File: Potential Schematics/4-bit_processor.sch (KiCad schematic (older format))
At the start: 0 parts

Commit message: Made Full ALU
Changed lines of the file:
@@
 $Descr A4 11693 8268
 encoding utf-8
-Sheet 1 6
+Sheet 1 22
 Title "4-bit_processor"
 Date "2018-09-11"
@@
 $EndDescr
 $Sheet
-S 1900 1250 750  1000
-U 5B990C59
-F0 "Full_ALU" 60
-F1 "Full_ALU.sch" 60
+S 1100 1200 3300 2300
+U 5B9D167A
+F0 "CPU" 60
+F1 "CPU.sch" 60
 $EndSheet
 $EndSCHEMATC

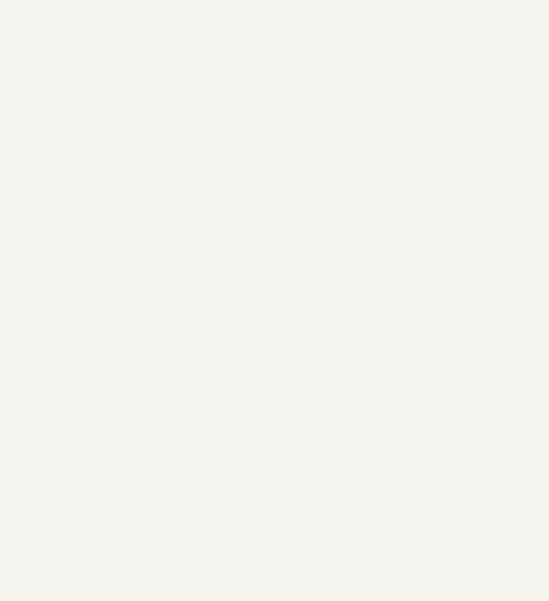
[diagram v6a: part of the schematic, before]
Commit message: Updated overview of Schematic
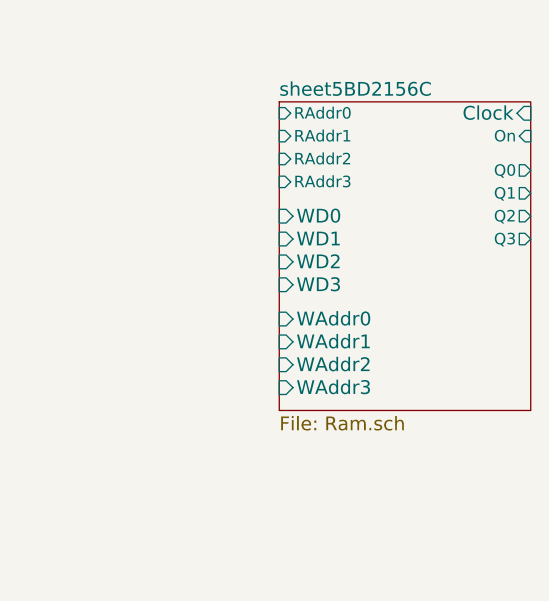
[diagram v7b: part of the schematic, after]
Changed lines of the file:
@@
 $Descr A4 11693 8268
 encoding utf-8
-Sheet 1 467
+Sheet 1 902
 Title "4-bit_processor"
 Date "2018-09-14"
@@
 F1 "CPU.sch" 60
 $EndSheet
+$Sheet
+S 6400 1450 1100 1350
+U 5BD21588
+F0 "sheet5BD2156C" 60
+F1 "Ram.sch" 60
+F2 "Clock" I R 7500 1500 60
+F3 "WD0" I L 6400 1950 60
+F4 "WD1" I L 6400 2050 60
+F5 "WD2" I L 6400 2150 60
+F6 "WD3" I L 6400 2250 60
+F7 "WAddr0" I L 6400 2400 60
+F8 "WAddr1" I L 6400 2500 60
+F9 "WAddr2" I L 6400 2600 60
+F10 "WAddr3" I L 6400 2700 60
+F11 "RAddr0" I L 6400 1500 50
+F12 "RAddr1" I L 6400 1600 50
+F13 "RAddr2" I L 6400 1700 50
+F14 "RAddr3" I L 6400 1800 50
+F15 "Q0" O R 7500 1750 50
+F16 "Q1" O R 7500 1850 50
+F17 "Q2" O R 7500 1950 50
+F18 "Q3" O R 7500 2050 50
+F19 "On" I R 7500 1600 50
+$EndSheet
 $EndSCHEMATC

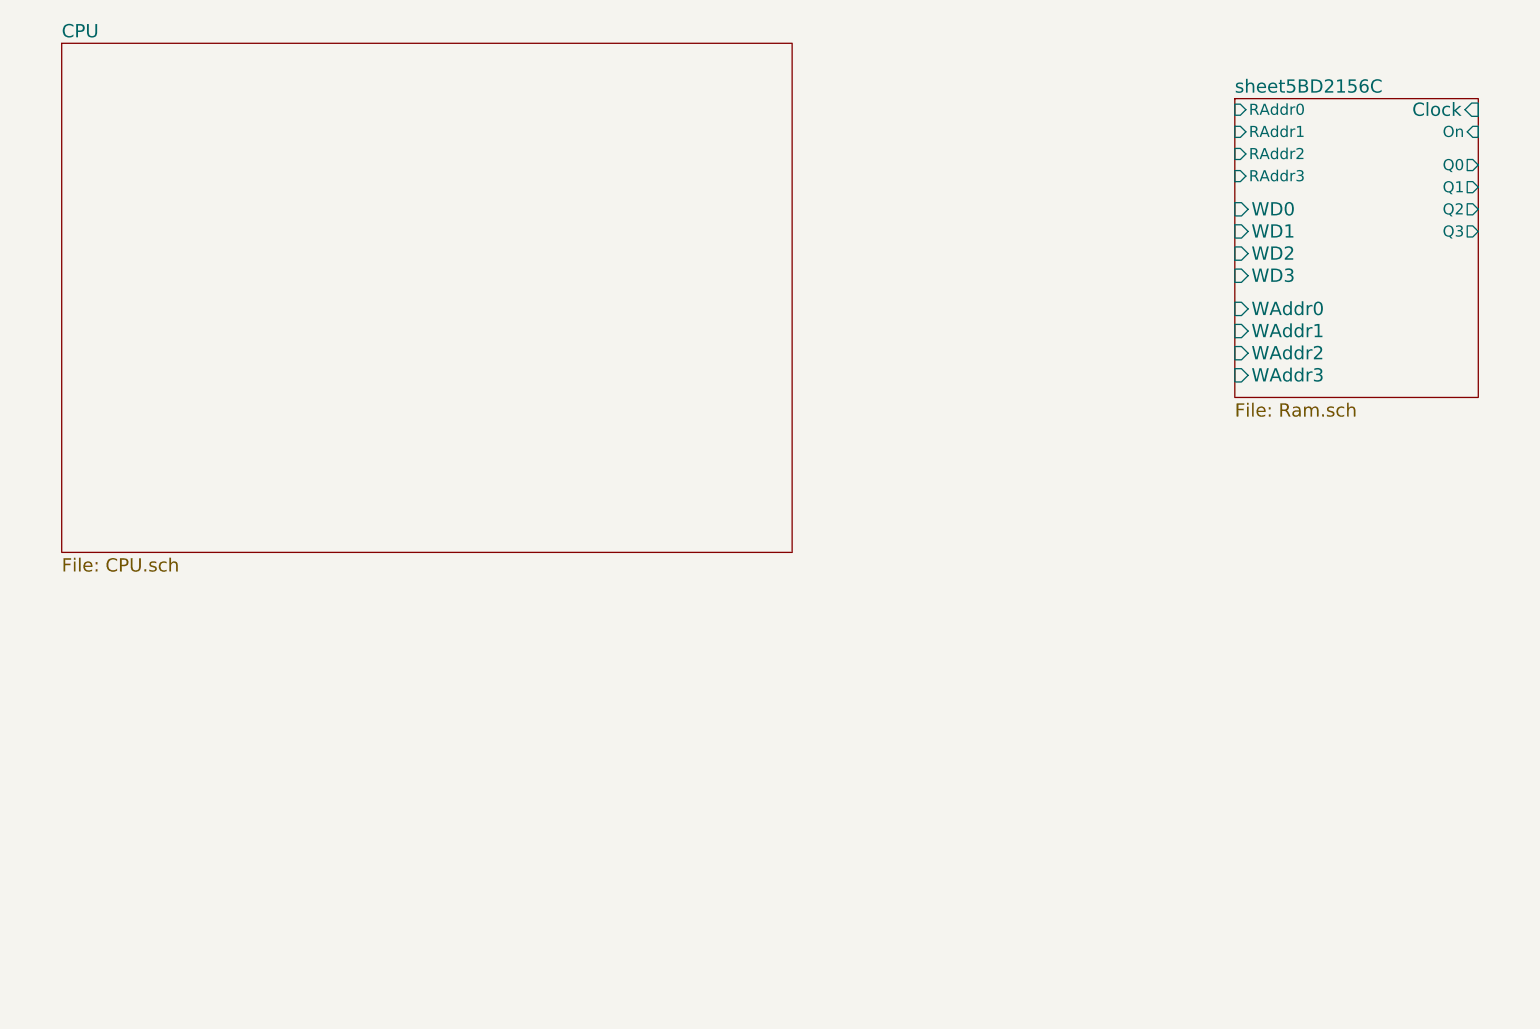
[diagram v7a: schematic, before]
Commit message: In the middle of adding ROM
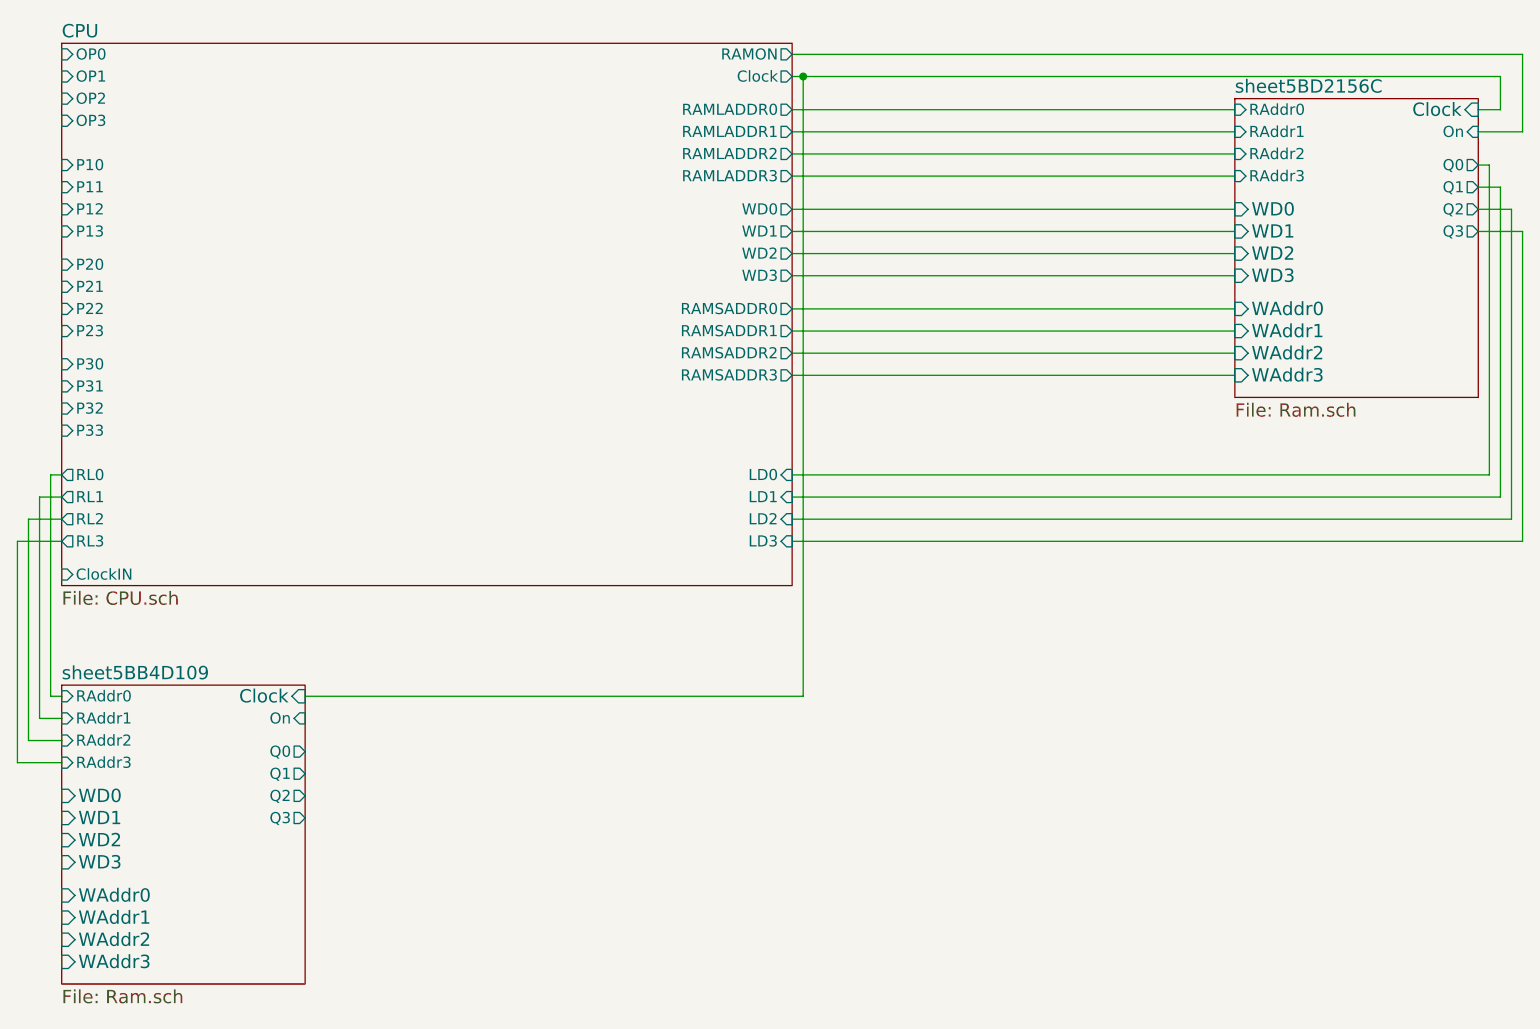
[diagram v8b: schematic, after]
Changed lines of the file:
@@
 $Descr A4 11693 8268
 encoding utf-8
-Sheet 1 902
+Sheet 1 1330
 Title "4-bit_processor"
 Date "2018-09-14"
@@
 $EndDescr
 $Sheet
-S 1100 1200 3300 2300
+S 1100 1200 3300 2450
 U 5B9D167A
 F0 "CPU" 60
 F1 "CPU.sch" 60
+F2 "OP0" I L 1100 1250 50
+F3 "OP1" I L 1100 1350 50
+F4 "OP2" I L 1100 1450 50
+F5 "OP3" I L 1100 1550 50
+F6 "P10" I L 1100 1750 50
+F7 "P11" I L 1100 1850 50
+F8 "P12" I L 1100 1950 50
+F9 "P13" I L 1100 2050 50
+F10 "P20" I L 1100 2200 50
+F11 "P21" I L 1100 2300 50
+F12 "P22" I L 1100 2400 50
+F13 "P23" I L 1100 2500 50
+F14 "P30" I L 1100 2650 50
+F15 "P31" I L 1100 2750 50
+F16 "P32" I L 1100 2850 50
+F17 "P33" I L 1100 2950 50
+F18 "WD0" O R 4400 1950 50
+F19 "WD1" O R 4400 2050 50
+F20 "WD2" O R 4400 2150 50
+F21 "WD3" O R 4400 2250 50
+F22 "LD0" I R 4400 3150 50
+F23 "LD1" I R 4400 3250 50
+F24 "LD2" I R 4400 3350 50
+F25 "LD3" I R 4400 3450 50
+F26 "RAMSADDR0" O R 4400 2400 50
+F27 "RAMLADDR0" O R 4400 1500 50
+F28 "RAMSADDR1" O R 4400 2500 50
+F29 "RAMSADDR2" O R 4400 2600 50
+F30 "RAMSADDR3" O R 4400 2700 50
+F31 "RAMLADDR1" O R 4400 1600 50
+F32 "RAMLADDR2" O R 4400 1700 50
+F33 "RAMLADDR3" O R 4400 1800 50
+F34 "RAMON" O R 4400 1250 50
+F35 "Clock" O R 4400 1350 50
+F36 "RL0" O L 1100 3150 50
+F37 "RL1" O L 1100 3250 50
+F38 "RL2" O L 1100 3350 50
+F39 "RL3" O L 1100 3450 50
+F40 "ClockIN" I L 1100 3600 50
 $EndSheet
 $Sheet
@@
 F19 "On" I R 7500 1600 50
 $EndSheet
+Wire Wire Line
+	4400 1950 6400 1950
+Wire Wire Line
+	6400 2050 4400 2050
+Wire Wire Line
+	4400 2150 6400 2150
+Wire Wire Line
+	6400 2250 4400 2250
+Wire Wire Line
+	4400 1500 6400 1500
+Wire Wire Line
+	6400 1600 4400 1600
+Wire Wire Line
+	4400 1700 6400 1700
+Wire Wire Line
+	6400 1800 4400 1800
+Wire Wire Line
+	4400 1350 4450 1350
+Wire Wire Line
+	7600 1350 7600 1500
+Wire Wire Line
+	7600 1500 7500 1500
+Wire Wire Line
+	7500 1600 7700 1600
+Wire Wire Line
+	7700 1600 7700 1250
+Wire Wire Line
+	7700 1250 4400 1250
+Wire Wire Line
+	4400 2400 6400 2400
+Wire Wire Line
+	6400 2500 4400 2500
+Wire Wire Line
+	4400 2600 6400 2600
+Wire Wire Line
+	6400 2700 4400 2700
+Wire Wire Line
+	4400 3150 7550 3150
+Wire Wire Line
+	7550 3150 7550 1750
+Wire Wire Line
+	7550 1750 7500 1750
+Wire Wire Line
+	4400 3250 7600 3250
+Wire Wire Line
+	7600 3250 7600 1850
+Wire Wire Line
+	7600 1850 7500 1850
+Wire Wire Line
+	4400 3350 7650 3350
+Wire Wire Line
+	7650 3350 7650 1950
+Wire Wire Line
+	7650 1950 7500 1950
+Wire Wire Line
+	4400 3450 7700 3450
+Wire Wire Line
+	7700 3450 7700 2050
+Wire Wire Line
+	7700 2050 7500 2050
+$Sheet
+S 1100 4100 1100 1350
+U 5BB4D11D
+F0 "sheet5BB4D109" 60
+F1 "Ram.sch" 60
+F2 "Clock" I R 2200 4150 60
+F3 "WD0" I L 1100 4600 60
+F4 "WD1" I L 1100 4700 60
+F5 "WD2" I L 1100 4800 60
+F6 "WD3" I L 1100 4900 60
+F7 "WAddr0" I L 1100 5050 60
+F8 "WAddr1" I L 1100 5150 60
+F9 "WAddr2" I L 1100 5250 60
+F10 "WAddr3" I L 1100 5350 60
+F11 "RAddr0" I L 1100 4150 50
+F12 "RAddr1" I L 1100 4250 50
+F13 "RAddr2" I L 1100 4350 50
+F14 "RAddr3" I L 1100 4450 50
+F15 "Q0" O R 2200 4400 50
+F16 "Q1" O R 2200 4500 50
+F17 "Q2" O R 2200 4600 50
+F18 "Q3" O R 2200 4700 50
+F19 "On" I R 2200 4250 50
+$EndSheet
+Wire Wire Line
+	1100 4150 1050 4150
+Wire Wire Line
+	1050 4150 1050 3150
+Wire Wire Line
+	1050 3150 1100 3150
+Wire Wire Line
+	1100 3250 1000 3250
+Wire Wire Line
+	1000 3250 1000 4250
+Wire Wire Line
+	1000 4250 1100 4250
+Wire Wire Line
+	1100 4350 950  4350
+Wire Wire Line
+	950  4350 950  3350
+Wire Wire Line
+	950  3350 1100 3350
+Wire Wire Line
+	1100 4450 900  4450
+Wire Wire Line
+	900  4450 900  3450
+Wire Wire Line
+	900  3450 1100 3450
+Wire Wire Line
+	4450 1350 4450 4150
+Wire Wire Line
+	4450 4150 2200 4150
+Connection ~ 4450 1350
+Wire Wire Line
+	4450 1350 7600 1350
 $EndSCHEMATC
